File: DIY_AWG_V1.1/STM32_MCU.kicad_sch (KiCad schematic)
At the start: 25 parts, among them J1 Conn_01x04_Pin, SW1 SW_Push, SW2 SW_Push, U10 STM32G473VETx, U8 USBLC6-2SC6, U9 161N-4BVS11, X1 SX2M8.000B10F20TNN

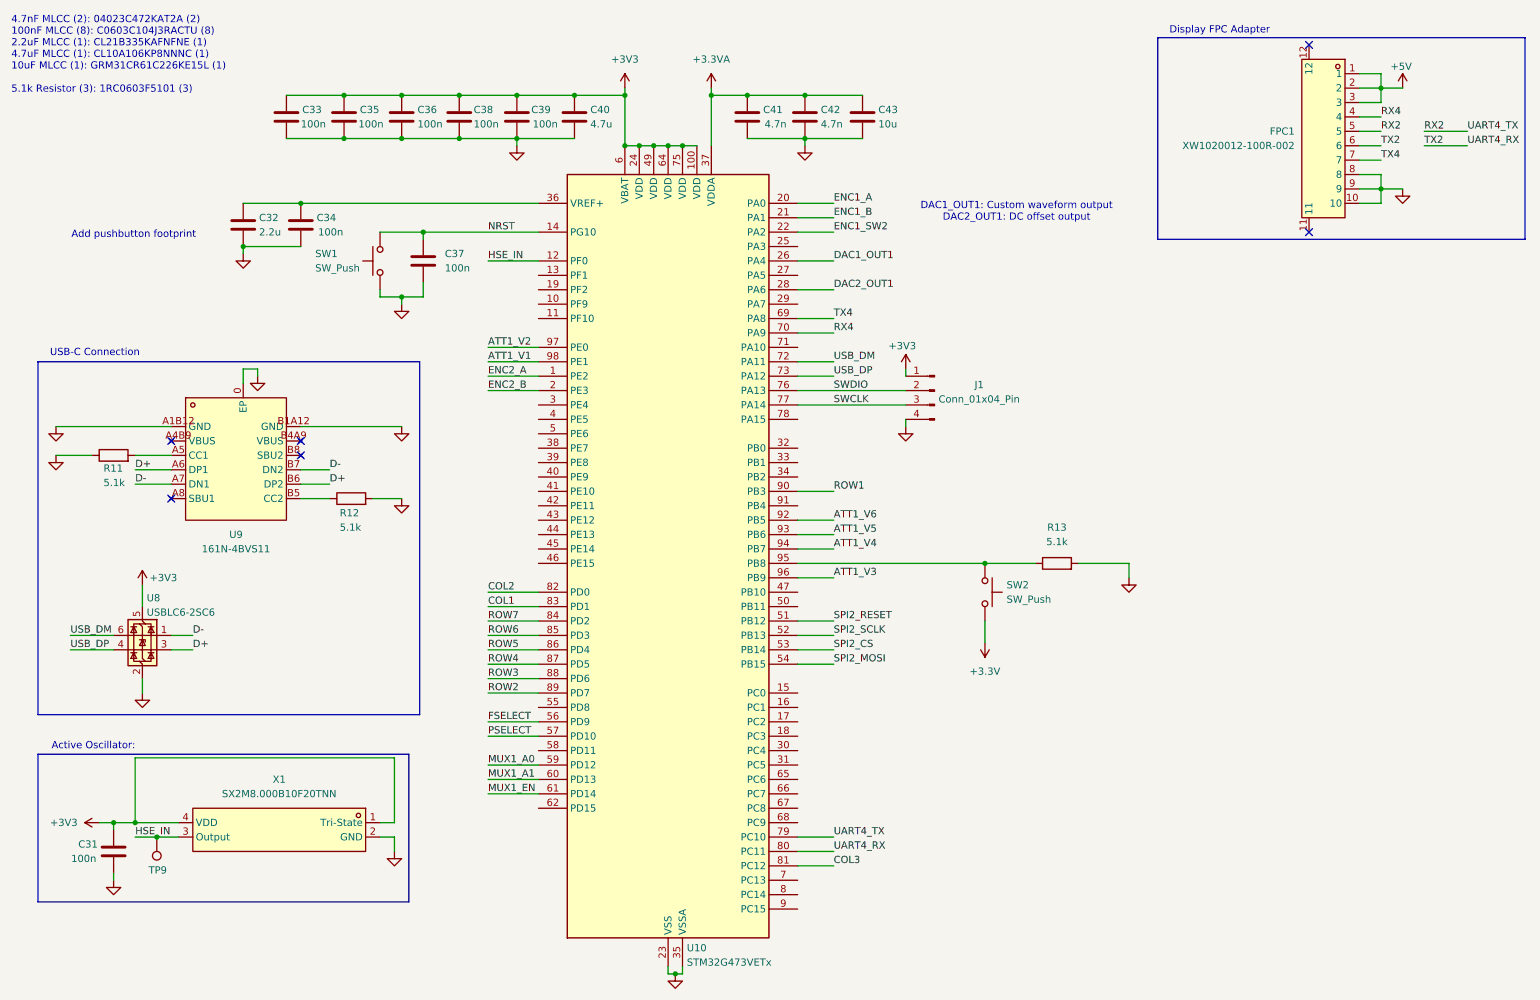
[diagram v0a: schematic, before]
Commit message: Updated pin description of relevant components
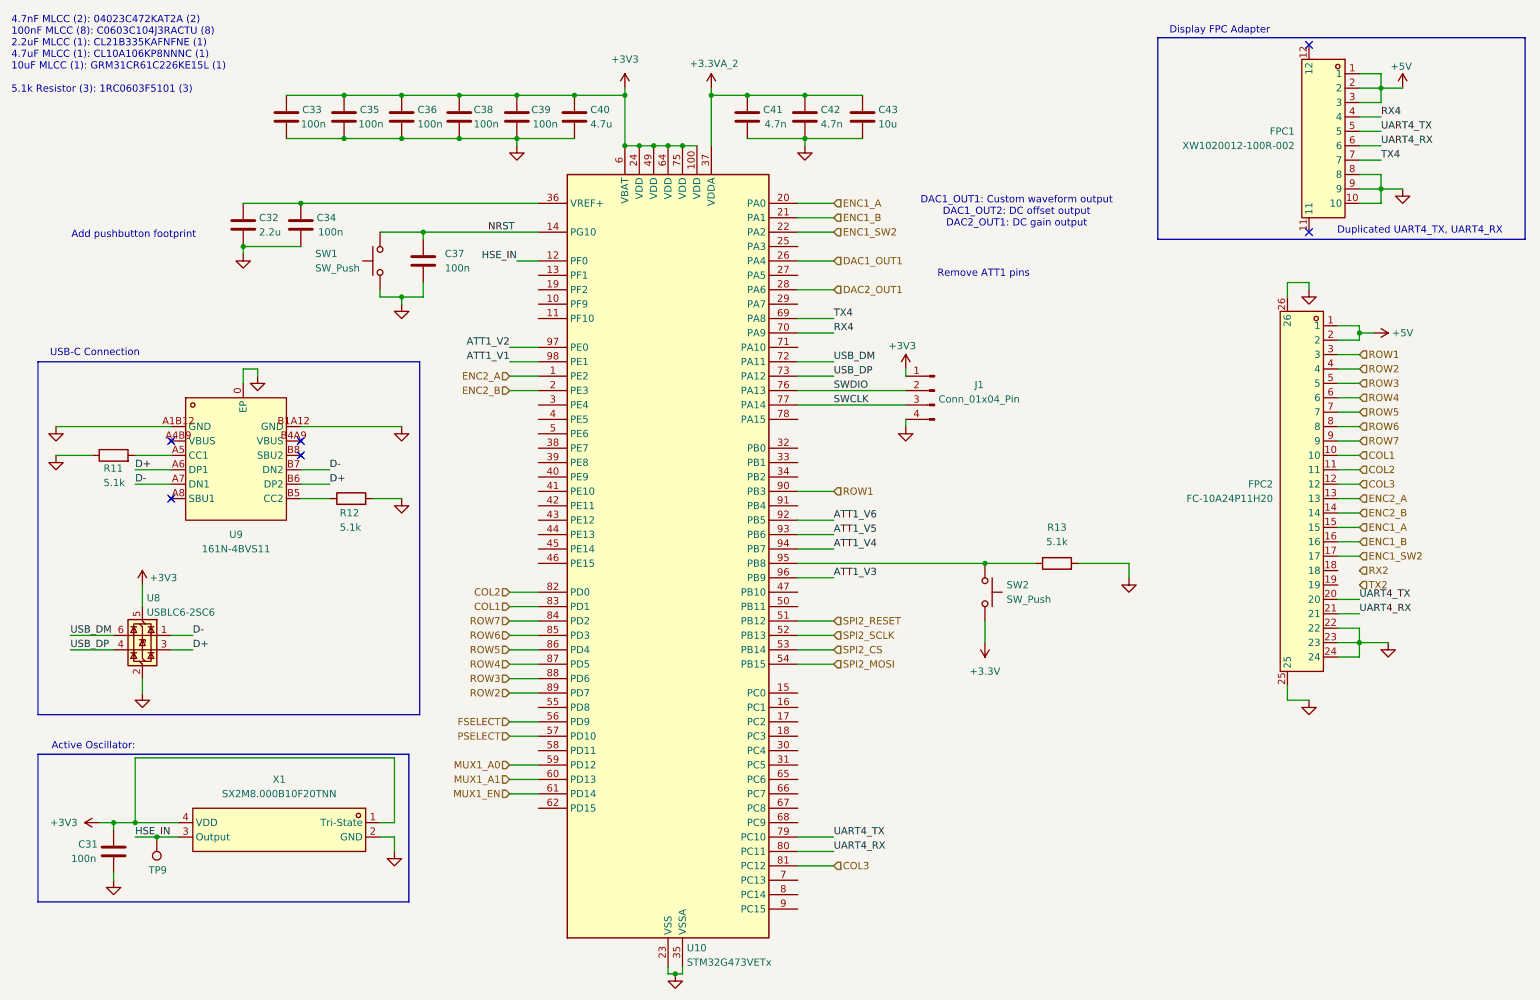
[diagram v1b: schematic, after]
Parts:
- added FPC2: FC-10A24P11H20, easyeda2kicad:FPC-SMD_24P-P1.00_FC-10A24P11H20, symbol easyeda2kicad:FC-10A24P11H20
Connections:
- net +5V: now also FPC2.1, FPC2.2
- net COL1: now also FPC2.10
- net COL2: now also FPC2.11
- net COL3: now also FPC2.12
- net ENC1_A: now also FPC2.15
- net ENC1_B: now also FPC2.16
- net ENC1_SW2: now also FPC2.17
- net ENC2_A: now also FPC2.13
- net ENC2_B: now also FPC2.14
- net GND: now also FPC2.22, FPC2.23, FPC2.24, FPC2.25, FPC2.26
- net ROW1: now also FPC2.3
- net ROW2: now also FPC2.4
- net ROW3: now also FPC2.5
- net ROW4: now also FPC2.6
- net ROW5: now also FPC2.7
- net ROW6: now also FPC2.8
- net ROW7: now also FPC2.9
- net RX2: no longer FPC1.5, U10.79 (PC10)
- net TX2: no longer FPC1.6, U10.80 (PC11)
- net +3.3VA renamed +3.3VA_2
- new net UART4_RX: FPC1.6, FPC2.21, U10.80 (PC11)
- new net UART4_TX: FPC1.5, FPC2.20, U10.79 (PC10)
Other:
- note added: "DAC1_OUT1: Custom waveform output DAC1_OUT2: DC offset output DAC2_OUT1: DC gain output"
- note added: "Duplicated UART4_TX, UART4_RX"
- note added: "Remove ATT1 pins"
- note removed: "DAC1_OUT1: Custom waveform output DAC2_OUT1: DC offset output"

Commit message: Updated schematics to clear ERCs
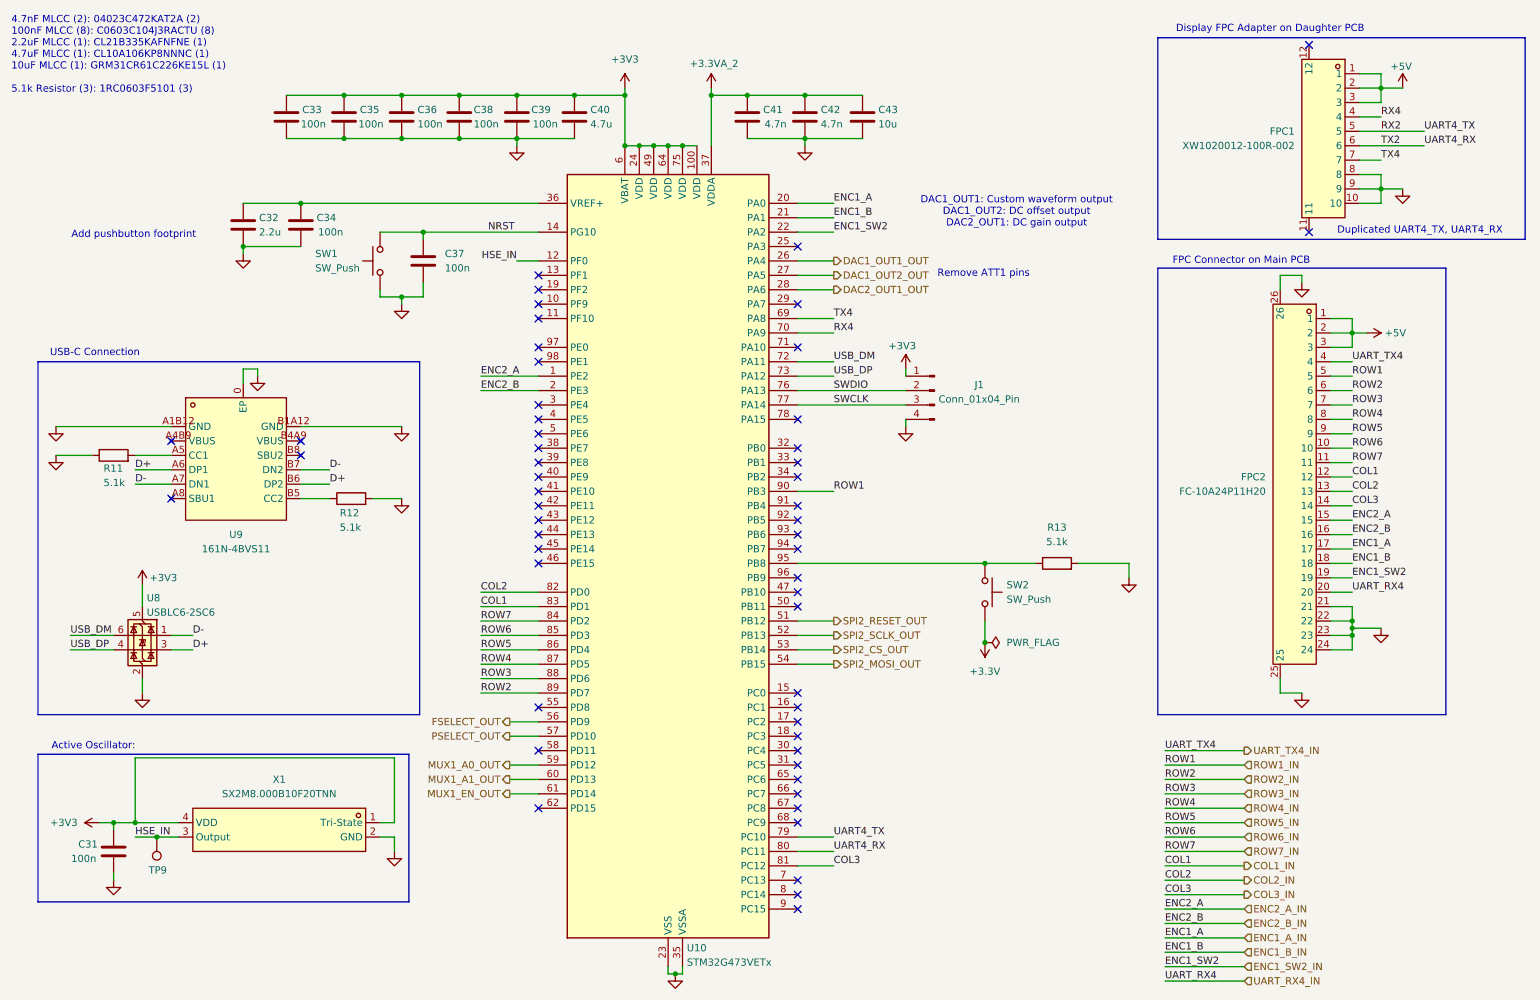
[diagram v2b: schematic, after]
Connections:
- net +5V: now also FPC2.3
- net GND: now also FPC2.21
- net RX2: now also FPC1.5, U10.79 (PC10)
- net TX2: now also FPC1.6, U10.80 (PC11)
- net ENC1_B_IN: now reaches FPC2.18
- net ENC1_B_IN: now also U10.21 (PA1)
- net ENC1_SW2_IN: now reaches FPC2.19
- net ENC1_SW2_IN: now also U10.22 (PA2)
- net DAC1_OUT2_OUT: now reaches U10.27 (PA5)
- net ATT1_V1: no longer names the net of U10.98 (PE1)
- net ATT1_V2: no longer names the net of U10.97 (PE0)
- net ATT1_V3: no longer names the net of U10.96 (PB9)
- net ATT1_V4: no longer names the net of U10.94 (PB7)
- net ATT1_V5: no longer names the net of U10.93 (PB6)
- net ATT1_V6: no longer names the net of U10.92 (PB5)
- net COL1 renamed COL1_IN
- net COL1_IN: now also FPC2.12; no longer FPC2.10
- net COL2 renamed COL2_IN
- net COL2_IN: now also FPC2.13; no longer FPC2.11
- net COL3 renamed COL3_IN
- net COL3_IN: now also FPC2.14; no longer FPC2.12
- net DAC1_OUT1 renamed DAC1_OUT1_OUT
- net DAC2_OUT1 renamed DAC2_OUT1_OUT
- net ENC1_A renamed ENC1_A_IN
- net ENC1_A_IN: now also FPC2.17; no longer FPC2.15
- net ENC1_B renamed ENC2_B_IN
- net ENC2_B_IN: now also U10.2 (PE3); no longer U10.21 (PA1)
- removed net ENC1_SW2: FPC2.17, U10.22 (PA2)
- net ENC2_A renamed ENC2_A_IN
- net ENC2_A_IN: now also FPC2.15; no longer FPC2.13
- removed net ENC2_B: FPC2.14, U10.2 (PE3)
- net FSELECT renamed FSELECT_OUT
- net MUX1_A0 renamed MUX1_A0_OUT
- net MUX1_A1 renamed MUX1_A1_OUT
- net MUX1_EN renamed MUX1_EN_OUT
- net PSELECT renamed PSELECT_OUT
- net ROW1 renamed ROW1_IN
- net ROW1_IN: now also FPC2.5; no longer FPC2.3
- net ROW2 renamed ROW2_IN
- net ROW2_IN: now also FPC2.6; no longer FPC2.4
- net ROW3 renamed ROW3_IN
- net ROW3_IN: now also FPC2.7; no longer FPC2.5
- net ROW4 renamed ROW4_IN
- net ROW4_IN: now also FPC2.8; no longer FPC2.6
- net ROW5 renamed ROW5_IN
- net ROW5_IN: now also FPC2.9; no longer FPC2.7
- net ROW6 renamed ROW6_IN
- net ROW6_IN: now also FPC2.10; no longer FPC2.8
- net ROW7 renamed ROW7_IN
- net ROW7_IN: now also FPC2.11; no longer FPC2.9
- net SPI2_CS renamed SPI2_CS_OUT
- net SPI2_MOSI renamed SPI2_MOSI_OUT
- net SPI2_RESET renamed SPI2_RESET_OUT
- net SPI2_SCLK renamed SPI2_SCLK_OUT
- removed net UART4_RX: FPC1.6, FPC2.21, U10.80 (PC11)
- removed net UART4_TX: FPC1.5, FPC2.20, U10.79 (PC10)
- new net UART_RX4_IN: FPC2.20
- new net UART_TX4_IN: FPC2.4
- no-connect marks 6 -> 54
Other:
- note added: "Display FPC Adapter on Daughter PCB"
- note added: "FPC Connector on Main PCB"
- note removed: "Display FPC Adapter"

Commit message: Updated schematics to clear ERCs
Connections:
- net COL1_IN renamed COL1
- net COL2_IN renamed COL2
- net COL3_IN renamed COL3
- net DAC1_OUT1_OUT renamed DAC1_OUT1
- net DAC1_OUT2_OUT renamed DAC1_OUT2
- net DAC2_OUT1_OUT renamed DAC2_OUT1
- net ENC1_A_IN renamed ENC1_A
- net ENC1_B_IN renamed ENC1_B
- net ENC1_SW2_IN renamed ENC1_SW2
- net ENC2_A_IN renamed ENC2_A
- net ENC2_B_IN renamed ENC2_B
- net FSELECT_OUT renamed FSELECT
- net MUX1_A0_OUT renamed MUX1_A0
- net MUX1_A1_OUT renamed MUX1_A1
- net MUX1_EN_OUT renamed MUX1_EN
- net PSELECT_OUT renamed PSELECT
- net ROW1_IN renamed ROW1
- net ROW2_IN renamed ROW2
- net ROW3_IN renamed ROW3
- net ROW4_IN renamed ROW4
- net ROW5_IN renamed ROW5
- net ROW6_IN renamed ROW6
- net ROW7_IN renamed ROW7
- net RX2 renamed UART4_TX
- net SPI2_CS_OUT renamed SPI2_CS
- net SPI2_MOSI_OUT renamed SPI2_MOSI
- net SPI2_RESET_OUT renamed SPI2_RESET
- net SPI2_SCLK_OUT renamed SPI2_SCLK
- net TX2 renamed UART4_RX
- net UART_RX4_IN renamed UART_RX4
- net UART_TX4_IN renamed UART_TX4
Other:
- note added: "RX2"
- note added: "TX2"
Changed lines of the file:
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@@
 		)
 	)
+	(text "TX2"
+		(exclude_from_sim no)
+		(at 270.51 35.56 0)
+		(effects
+			(font
+				(size 1.27 1.27)
+			)
+		)
+	)
 	(text "4.7nF MLCC (2): 04023C472KAT2A (2)\n100nF MLCC (8): C0603C104J3RACTU (8)\n2.2uF MLCC (1): CL21B335KAFNFNE (1)\n4.7uF MLCC (1): CL10A106KP8NNNC (1)\n10uF MLCC (1): GRM31CR61C226KE15L (1)\n\n5.1k Resistor (3): 1RC0603F5101 (3)"
 		(exclude_from_sim no)
@@
 		)
 	)
+	(text "RX2\n"
+		(exclude_from_sim no)
+		(at 270.51 33.02 0)
+		(effects
+			(font
+				(size 1.27 1.27)
+			)
+		)
+	)
 	(text "DAC1_OUT1: Custom waveform output\nDAC1_OUT2: DC offset output\nDAC2_OUT1: DC gain output"
 		(exclude_from_sim no)
@@
 	(wire
 		(pts
-			(xy 254 34.29) (xy 265.43 34.29)
+			(xy 254 34.29) (xy 257.81 34.29)
 		)
 		(stroke
@@
 	(wire
 		(pts
-			(xy 254 36.83) (xy 265.43 36.83)
+			(xy 254 36.83) (xy 257.81 36.83)
 		)
 		(stroke
@@
 		)
 	)
-	(label "TX2"
-		(at 257.81 36.83 0)
-		(effects
-			(font
-				(size 1.27 1.27)
-			)
-			(justify left bottom)
-		)
-	)
 	(label "ENC2_A"
 		(at 252.73 102.87 0)
@@
 	)
 	(label "UART4_TX"
-		(at 265.43 34.29 0)
+		(at 257.81 34.29 0)
 		(effects
 			(font
@@
 		)
 	)
-	(label "RX2"
-		(at 257.81 34.29 0)
-		(effects
-			(font
-				(size 1.27 1.27)
-			)
-			(justify left bottom)
-		)
-	)
 	(label "ROW3"
 		(at 252.73 82.55 0)
@@
 	)
 	(label "UART4_RX"
-		(at 265.43 36.83 0)
+		(at 257.81 36.83 0)
 		(effects
 			(font
@@
 		)
 	)
-	(hierarchical_label "DAC1_OUT2_OUT"
+	(hierarchical_label "DAC1_OUT2"
 		(shape output)
 		(at 161.29 59.69 0)
@@
 		)
 	)
-	(hierarchical_label "ENC2_A_IN"
+	(hierarchical_label "ENC2_A"
 		(shape input)
 		(at 233.68 171.45 0)
@@
 		)
 	)
-	(hierarchical_label "DAC2_OUT1_OUT"
+	(hierarchical_label "DAC2_OUT1"
 		(shape output)
 		(at 161.29 62.23 0)
@@
 		)
 	)
-	(hierarchical_label "SPI2_RESET_OUT"
+	(hierarchical_label "SPI2_RESET"
 		(shape output)
 		(at 161.29 120.65 0)
@@
 		)
 	)
-	(hierarchical_label "ROW1_IN"
+	(hierarchical_label "ROW1"
 		(shape input)
 		(at 233.68 146.05 0)
@@
 		)
 	)
-	(hierarchical_label "COL3_IN"
+	(hierarchical_label "COL3"
 		(shape output)
 		(at 233.68 168.91 0)
@@
 		)
 	)
-	(hierarchical_label "MUX1_EN_OUT"
+	(hierarchical_label "MUX1_EN"
 		(shape output)
 		(at 104.14 151.13 180)
@@
 		)
 	)
-	(hierarchical_label "ENC2_B_IN"
+	(hierarchical_label "ENC2_B"
 		(shape input)
 		(at 233.68 173.99 0)
@@
 		)
 	)
-	(hierarchical_label "ROW6_IN"
+	(hierarchical_label "ROW6"
 		(shape input)
 		(at 233.68 158.75 0)
@@
 		)
 	)
-	(hierarchical_label "ROW7_IN"
+	(hierarchical_label "ROW7"
 		(shape input)
 		(at 233.68 161.29 0)
@@
 		)
 	)
-	(hierarchical_label "UART_TX4_IN"
+	(hierarchical_label "UART_TX4"
 		(shape output)
 		(at 233.68 143.51 0)
@@
 		)
 	)
-	(hierarchical_label "DAC1_OUT1_OUT"
+	(hierarchical_label "DAC1_OUT1"
 		(shape output)
 		(at 161.29 57.15 0)
@@
 		)
 	)
-	(hierarchical_label "ROW3_IN"
+	(hierarchical_label "ROW3"
 		(shape input)
 		(at 233.68 151.13 0)
@@
 		)
 	)
-	(hierarchical_label "MUX1_A0_OUT"
+	(hierarchical_label "MUX1_A0"
 		(shape output)
 		(at 104.14 146.05 180)
@@
 		)
 	)
-	(hierarchical_label "MUX1_A1_OUT"
+	(hierarchical_label "MUX1_A1"
 		(shape output)
 		(at 104.14 148.59 180)
@@
 		)
 	)
-	(hierarchical_label "COL1_IN"
+	(hierarchical_label "COL1"
 		(shape output)
 		(at 233.68 163.83 0)
@@
 		)
 	)
-	(hierarchical_label "UART_RX4_IN"
+	(hierarchical_label "UART_RX4"
 		(shape input)
 		(at 233.68 184.15 0)
@@
 		)
 	)
-	(hierarchical_label "ROW5_IN"
+	(hierarchical_label "ROW5"
 		(shape input)
 		(at 233.68 156.21 0)
@@
 		)
 	)
-	(hierarchical_label "ENC1_A_IN"
+	(hierarchical_label "ENC1_A"
 		(shape input)
 		(at 233.68 176.53 0)
@@
 		)
 	)
-	(hierarchical_label "COL2_IN"
+	(hierarchical_label "COL2"
 		(shape output)
 		(at 233.68 166.37 0)
@@
 		)
 	)
-	(hierarchical_label "SPI2_SCLK_OUT"
+	(hierarchical_label "SPI2_SCLK"
 		(shape output)
 		(at 161.29 123.19 0)
@@
 		)
 	)
-	(hierarchical_label "FSELECT_OUT"
+	(hierarchical_label "FSELECT"
 		(shape output)
 		(at 104.14 138.43 180)
@@
 		)
 	)
-	(hierarchical_label "PSELECT_OUT"
+	(hierarchical_label "PSELECT"
 		(shape output)
 		(at 104.14 140.97 180)
@@
 		)
 	)
-	(hierarchical_label "SPI2_CS_OUT"
+	(hierarchical_label "SPI2_CS"
 		(shape output)
 		(at 161.29 125.73 0)
@@
 		)
 	)
-	(hierarchical_label "ROW4_IN"
+	(hierarchical_label "ROW4"
 		(shape input)
 		(at 233.68 153.67 0)
@@
 		)
 	)
-	(hierarchical_label "ROW2_IN"
+	(hierarchical_label "ROW2"
 		(shape input)
 		(at 233.68 148.59 0)
@@
 		)
 	)
-	(hierarchical_label "SPI2_MOSI_OUT"
+	(hierarchical_label "SPI2_MOSI"
 		(shape output)
 		(at 161.29 128.27 0)
@@
 		)
 	)
-	(hierarchical_label "ENC1_SW2_IN"
+	(hierarchical_label "ENC1_SW2"
 		(shape input)
 		(at 233.68 181.61 0)
@@
 		)
 	)
-	(hierarchical_label "ENC1_B_IN"
+	(hierarchical_label "ENC1_B"
 		(shape input)
 		(at 233.68 179.07 0)

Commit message: Updated component footprints
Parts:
- added TP10, TP11: TestPoint, symbol Connector:TestPoint
- renumbered FPC2 to FPC1, FPC1 to FPC2
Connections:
- net +3V3: no longer U8.5 (VBUS)
- net UART4_RX: now also TP11.1
- net UART4_TX: now also TP10.1
- net VBUS: now reaches U9.A4B9 (VBUS)
- net VBUS: now also U8.5 (VBUS), U9.B4A9 (VBUS)
- no-connect marks 54 -> 52
